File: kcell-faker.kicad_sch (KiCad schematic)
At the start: 22 parts, among them J2 USB_C_Receptacle_USB2.0, J3 Conn_ARM_JTAG_SWD_10, SW1 PWR, U2 SRV05-4, U4 STM32G431CBTx, U5 STM32F411CEUx, U6 ESP32-S3-MINI-1, U7 XC6206PxxxMR

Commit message: more mpns
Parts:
- added U3: ESP32-S3-WROOM-1, RF_Module:ESP32-S3-WROOM-1, symbol RF_Module:ESP32-S3-WROOM-1
- U6: MPN (none) -> ESP32-S3-MINI-1-N8 Copy; lcsc# (none) -> C2913206
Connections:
- new net: U3.1 (GND), U3.40 (GND), U3.41 (GND)
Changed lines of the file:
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@@
+			)
+		)
+		(property "MPN" "ESP32-S3-MINI-1-N8 Copy "
+			(at -22.86 170.18 0)
+			(effects
+				(font
+					(size 1.27 1.27)
+				)
+				(hide yes)
+			)
+		)
+		(property "lcsc#" "C2913206"
+			(at -22.86 170.18 0)
+			(effects
+				(font
+					(size 1.27 1.27)
+				)
+				(hide yes)
 			)
 		)
@@
 					(unit 1)
 				)
+			)
+		)
+	)
+	(symbol
+		(lib_id "RF_Module:ESP32-S3-WROOM-1")
+		(at -63.5 175.26 0)
+		(unit 1)
+		(exclude_from_sim no)
+		(in_bom yes)
+		(on_board yes)
+		(dnp no)
+		(fields_autoplaced yes)
+		(property "Reference" "U3"
+			(at -61.3059 144.78 0)
+			(effects
+				(font
+					(size 1.27 1.27)
+				)
+				(justify left)
+			)
+		)
+		(property "Value" "ESP32-S3-WROOM-1"
+			(at -61.3059 147.32 0)
+			(effects
+				(font
+					(size 1.27 1.27)
+				)
+				(justify left)
+			)
+		)
+		(property "Footprint" "RF_Module:ESP32-S3-WROOM-1"
+			(at -63.5 172.72 0)
+			(effects
+				(font
+					(size 1.27 1.27)
+				)
+				(hide yes)
+			)
+		)
+		(property "Datasheet" "https://www.espressif.com/sites/default/files/documentation/esp32-s3-wroom-1_wroom-1u_datasheet_en.pdf"
+			(at -63.5 175.26 0)
+			(effects
+				(font
+					(size 1.27 1.27)
+				)
+				(hide yes)
+			)
+		)
+		(property "Description" "RF Module, ESP32-S3 SoC, Wi-Fi 802.11b/g/n, Bluetooth, BLE, 32-bit, 3.3V, onboard antenna, SMD"
+			(at -63.5 175.26 0)
+			(effects
+				(font
+					(size 1.27 1.27)
+				)
+				(hide yes)
+			)
+		)
+		(property "lcsc#" "C2913198"
+			(at -63.5 175.26 0)
+			(effects
+				(font
+					(size 1.27 1.27)
+				)
+				(hide yes)
+			)
+		)
+		(property "MPN" "ESP32-S3-WROOM-1-N8"
+			(at -63.5 175.26 0)
+			(effects
+				(font
+					(size 1.27 1.27)
+				)
+				(hide yes)
+			)
+		)
+		(pin "31"
+		)
+		(pin "17"
+		)
+		(pin "35"
+		)
+		(pin "4"
+		)
+		(pin "41"
+		)
+		(pin "40"
+		)
+		(pin "22"
+		)
+		(pin "37"
+		)
+		(pin "20"
+		)
+		(pin "25"
+		)
+		(pin "16"
+		)
+		(pin "8"
+		)
+		(pin "5"
+		)
+		(pin "36"
+		)
+		(pin "1"
+		)
+		(pin "12"
+		)
+		(pin "11"
+		)
+		(pin "10"
+		)
+		(pin "39"
+		)
+		(pin "27"
+		)
+		(pin "9"
+		)
+		(pin "13"
+		)
+		(pin "34"
+		)
+		(pin "7"
+		)
+		(pin "21"
+		)
+		(pin "32"
+		)
+		(pin "33"
+		)
+		(pin "38"
+		)
+		(pin "3"
+		)
+		(pin "18"
+		)
+		(pin "19"
+		)
+		(pin "2"
+		)
+		(pin "29"
+		)
+		(pin "23"
+		)
+		(pin "6"
+		)
+		(pin "24"
+		)
+		(pin "30"
+		)
+		(pin "15"
+		)
+		(pin "28"
+		)
+		(pin "14"
+		)
+		(pin "26"
+		)
+		(instances
+			(project ""
+				(path "/dc836b5d-e5fb-485d-8f74-ab331e55e69f"
+					(reference "U3")
+					(unit 1)
+				)

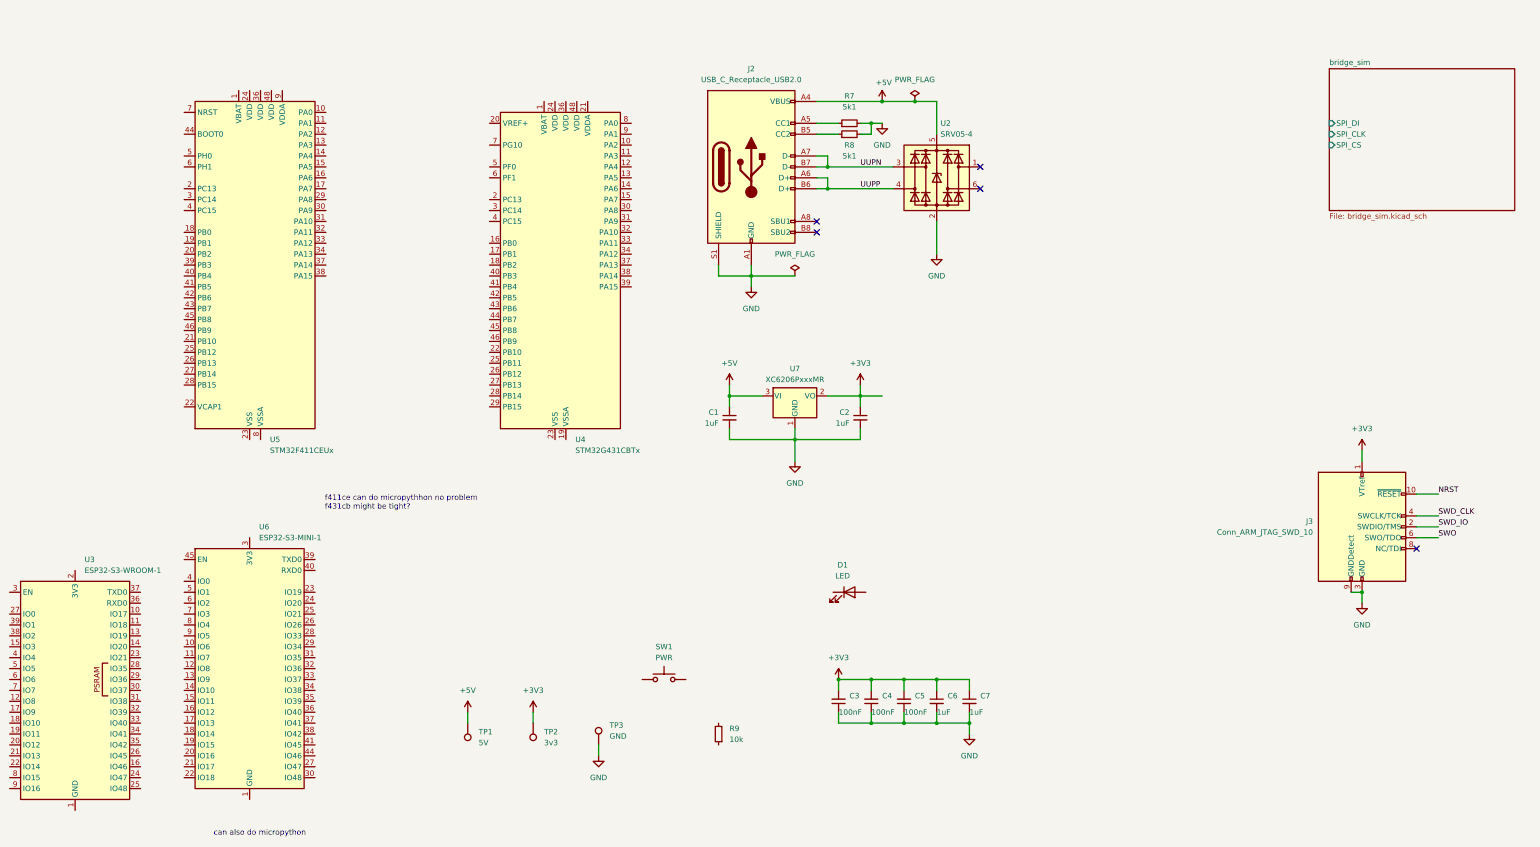
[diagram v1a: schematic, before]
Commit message: Preliminary check stage
most parts mounted, most parts filled. roughly placed for sanity.
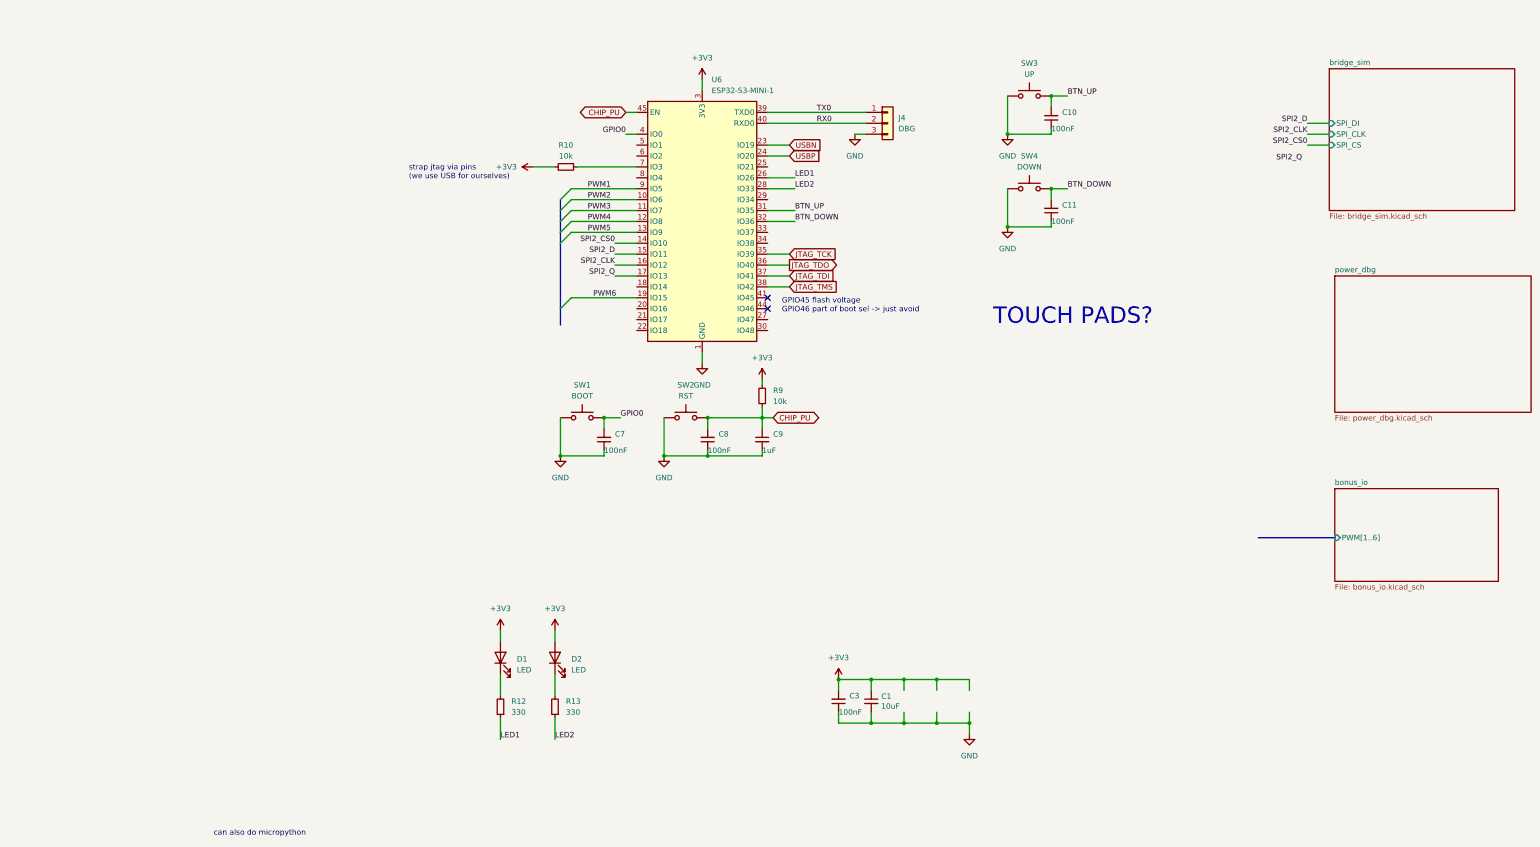
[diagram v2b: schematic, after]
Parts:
- removed C2, C6: 1uF, Capacitor_SMD:C_0603_1608Metric, symbol Device:C_Small
- removed C4, C5: 100nF, Capacitor_SMD:C_0603_1608Metric, symbol Device:C_Small
- removed J2: USB_C_Receptacle_USB2.0, Connector_USB:USB_C_Receptacle_G-Switch_GT-USB-7010ASV, symbol Connector:USB_C_Receptacle_USB2.0
- removed J3: Conn_ARM_JTAG_SWD_10, Connector_PinHeader_1.27mm:PinHeader_2x05_P1.27mm_Vertical_SMD, symbol Connector:Conn_ARM_JTAG_SWD_10
- removed R7, R8: 5k1, Resistor_SMD:R_0603_1608Metric, symbol Device:R_Small
- removed TP1: 5V, TestPoint:TestPoint_THTPad_D1.5mm_Drill0.7mm, symbol Connector:TestPoint
- removed TP2: 3v3, TestPoint:TestPoint_THTPad_D1.5mm_Drill0.7mm, symbol Connector:TestPoint
- removed TP3: GND, TestPoint:TestPoint_THTPad_D1.5mm_Drill0.7mm, symbol Connector:TestPoint
- removed U2: SRV05-4, Package_TO_SOT_SMD:SOT-23-6, symbol karl-parts:SRV05-4
- removed U3: ESP32-S3-WROOM-1, RF_Module:ESP32-S3-WROOM-1, symbol RF_Module:ESP32-S3-WROOM-1
- removed U4: STM32G431CBTx, Package_QFP:LQFP-48_7x7mm_P0.5mm, symbol MCU_ST_STM32G4:STM32G431CBTx
- removed U5: STM32F411CEUx, Package_DFN_QFN:QFN-48-1EP_7x7mm_P0.5mm_EP5.6x5.6mm, symbol MCU_ST_STM32F4:STM32F411CEUx
- removed U7: XC6206PxxxMR, Package_TO_SOT_SMD:SOT-23-3, symbol Regulator_Linear:XC6206PxxxMR
- added C10, C11, C8: 100nF, Capacitor_SMD:C_0603_1608Metric, symbol Device:C_Small
- added C9: 1uF, Capacitor_SMD:C_0603_1608Metric, symbol Device:C_Small
- added D2: LED, LED_SMD:LED_0603_1608Metric, symbol Device:LED
- added J4: DBG, Connector_PinHeader_2.54mm:PinHeader_1x03_P2.54mm_Vertical, symbol Connector_Generic:Conn_01x03
- added R10: 10k, Resistor_SMD:R_0603_1608Metric, symbol Device:R_Small
- added R12, R13: 330, Resistor_SMD:R_0603_1608Metric, symbol Device:R_Small
- added SW2: RST, Button_Switch_SMD:SW_SPST_TL3342, symbol Switch:SW_Push
- added SW3: UP, Button_Switch_SMD:SW_SPST_TL3342, symbol Switch:SW_Push
- added SW4: DOWN, Button_Switch_SMD:SW_SPST_TL3342, symbol Switch:SW_Push
- C1: value 1uF -> 10uF; footprint Capacitor_SMD:C_0603_1608Metric -> Capacitor_SMD:C_0805_2012Metric; MPN CL10A105KB8NNNC -> CL21A106KAYNNNE; jlcbasic basic -> (none); lcsc# C15849 -> C15850
- C7: value 1uF -> 100nF; MPN CL10A105KB8NNNC -> CC0603KRX7R9BB104; lcsc# C15849 -> C14663
- SW1: value PWR -> BOOT
- U6: MPN ESP32-S3-MINI-1-N8 Copy -> ESP32-S3-MINI-1-N8
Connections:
- net +5V is gone; now on net +3V3: C1.1
- net +3V3: now also D1.2 (A), R9.2, U6.3 (3V3), D2.2 (A), R10.2; no longer C7.1
- net GND: now also C7.1, SW1.1, U6.1 (GND), U6.2 (GND), U6.42 (GND), U6.43 (GND), U6.46 (GND), U6.47 (GND), U6.48 (GND), U6.49 (GND), U6.50 (GND), U6.51 (GND), U6.52 (GND), U6.53 (GND), U6.54 (GND), U6.55 (GND), U6.56 (GND), U6.57 (GND), U6.58 (GND), U6.59 (GND), U6.60 (GND), U6.61 (GND), U6.62 (GND), U6.63 (GND), U6.64 (GND), U6.65 (GND), C10.1, C11.1, C8.1, C9.2, J4.3 (Pin_3), SW2.1, SW3.1, SW4.1; no longer C7.2
- net PWM2: now reaches U6.10 (IO6)
- net PWM3: now reaches U6.11 (IO7)
- net PWM4: now reaches U6.12 (IO8)
- net PWM5: now reaches U6.13 (IO9)
- net SPI2_CS0: now reaches U6.14 (IO10)
- net SPI2_D: now reaches U6.15 (IO11)
- net SPI2_CLK: now reaches U6.16 (IO12)
- net SPI2_Q: now reaches U6.17 (IO13)
- net PWM6: now reaches U6.19 (IO15)
- net USBN: now reaches U6.23 (IO19)
- net USBP: now reaches U6.24 (IO20)
- net LED1: now reaches U6.26 (IO26)
- net LED1: now also R12.1
- net LED2: now reaches U6.28 (IO33)
- net LED2: now also R13.1
- net BTN_UP: now reaches U6.31 (IO35)
- net BTN_UP: now also C10.2, SW3.2
- net BTN_DOWN: now reaches U6.32 (IO36)
- net BTN_DOWN: now also C11.2, SW4.2
- net JTAG_TCK: now reaches U6.35 (IO39)
- net JTAG_TDO: now reaches U6.36 (IO40)
- net JTAG_TDI: now reaches U6.37 (IO41)
- net JTAG_TMS: now reaches U6.38 (IO42)
- net TX0: now reaches U6.39 (TXD0)
- net TX0: now also J4.1 (Pin_1)
- net GPIO0: now reaches U6.4 (IO0)
- net GPIO0: now also C7.2, SW1.2
- net RX0: now reaches U6.40 (RXD0)
- net RX0: now also J4.2 (Pin_2)
- net CHIP_PU: now reaches U6.45 (EN)
- net CHIP_PU: now also R9.1, C8.2, C9.1, SW2.2
- net at U6.7 (IO3): now also R10.1
- net PWM1: now reaches U6.9 (IO5)
- net at D1.1 (K): now also R12.2
- new net: D2.1 (K), R13.2
- no-connect marks 5 -> 2
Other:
- added sheet bonus_io (bonus_io.kicad_sch)
- added sheet power_dbg (power_dbg.kicad_sch)
- note added: "GPIO45 flash voltage GPIO46 part of boot sel -> just avoid"
- note added: "TOUCH PADS?"
- note added: "strap jtag via pins (we use USB for ourselves)"
- note removed: "f411ce can do micropythhon no problem f431cb might be tight?"
- moved on the sheet: D1, R9, SW1, U6

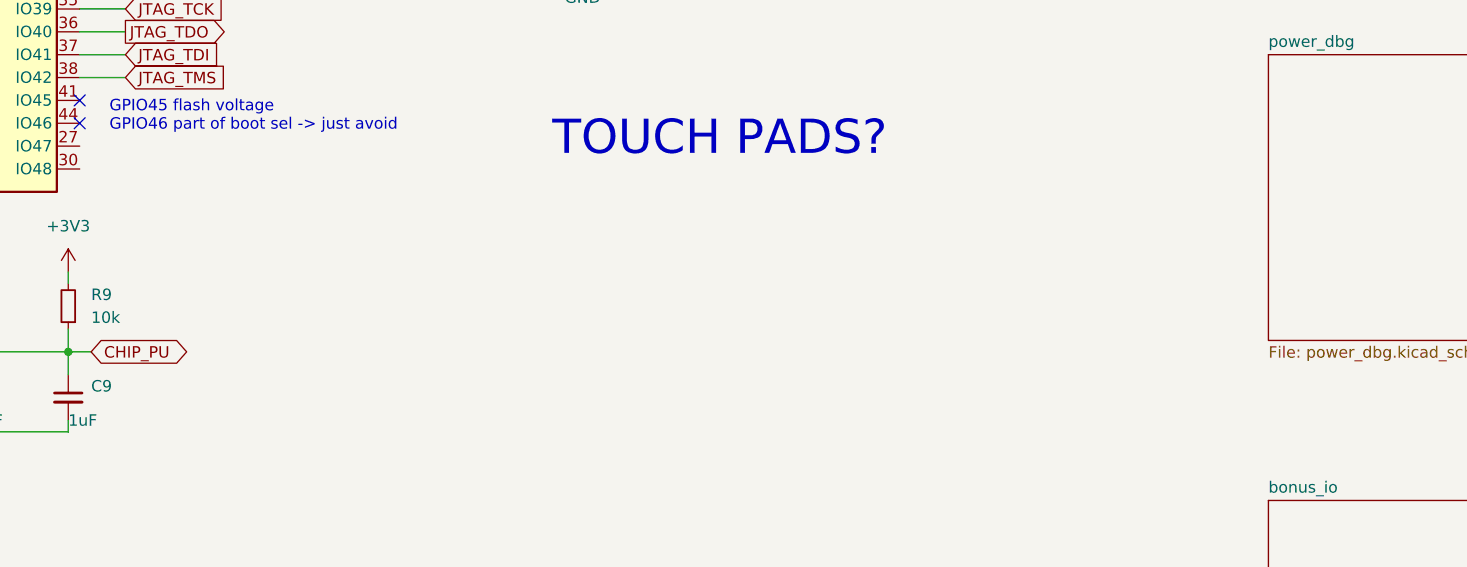
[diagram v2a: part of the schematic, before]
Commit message: Save current state
We're thinking of adding a second stage "fine" tune, because... why not!
We're at ~$60 assembled for 5 boards, with everything optional filled
in, so adding 5x$1 to have the second range seems "free"?
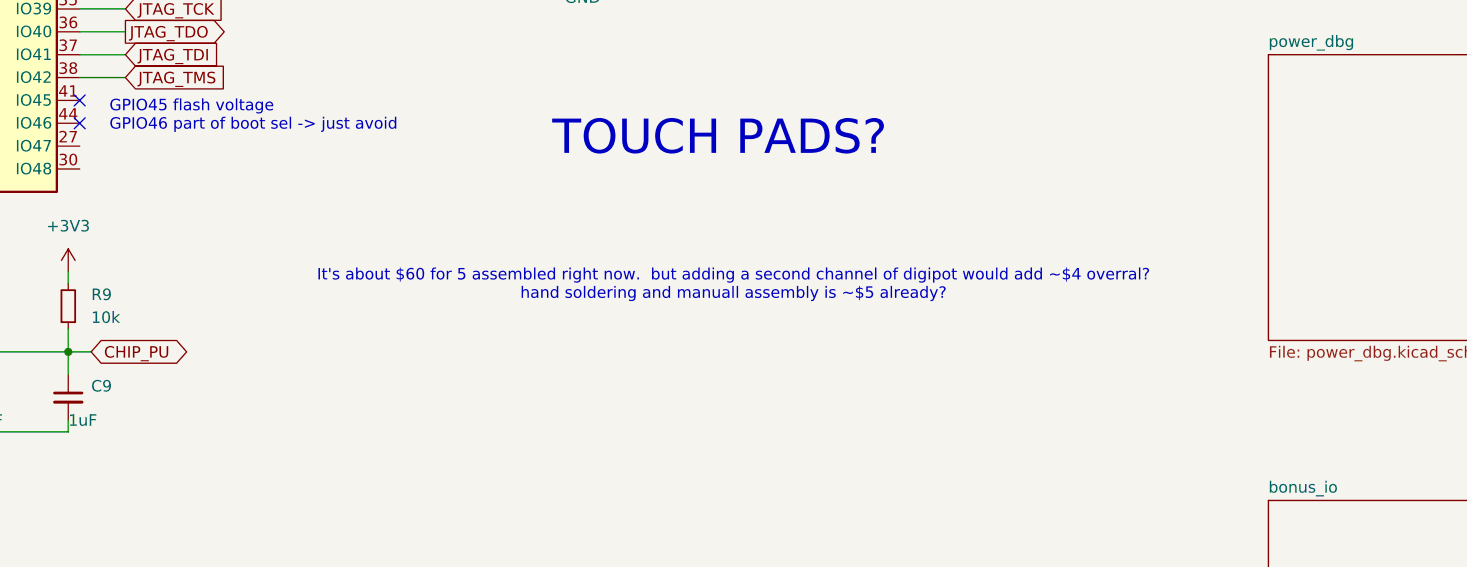
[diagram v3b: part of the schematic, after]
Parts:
- J4: lcsc# (none) -> C2937625
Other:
- note added: "It's about $60 for 5 assembled right now. but adding a second channel of digipot would add ~$4 overral? hand soldering and manuall assembly is ~$5 already?"
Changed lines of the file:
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@@
+		)
+	)
+	(text "It's about $60 for 5 assembled right now.  but adding a second channel of digipot would add ~$4 overral?\nhand soldering and manuall assembly is ~$5 already?"
+		(exclude_from_sim no)
+		(at 170.434 104.394 0)
+		(effects
+			(font
+				(size 1.27 1.27)
+			)
 		)
 	)
@@
 			(at 125.73 43.18 0)
 			(effects
+				(font
+					(size 1.27 1.27)
+				)
+				(hide yes)
+			)
+		)
+		(property "lcsc#" "C2937625"
+			(at 125.73 43.18 0)
+			(effects
